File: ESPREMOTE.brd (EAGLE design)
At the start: 47 x 78 mm, 38 parts, among them IC1 ESP12SMT, J1 2.1MM DC Jack, Q1 2N7002, Q2 2N7002, Q3 2N7002, Q4 2N7002

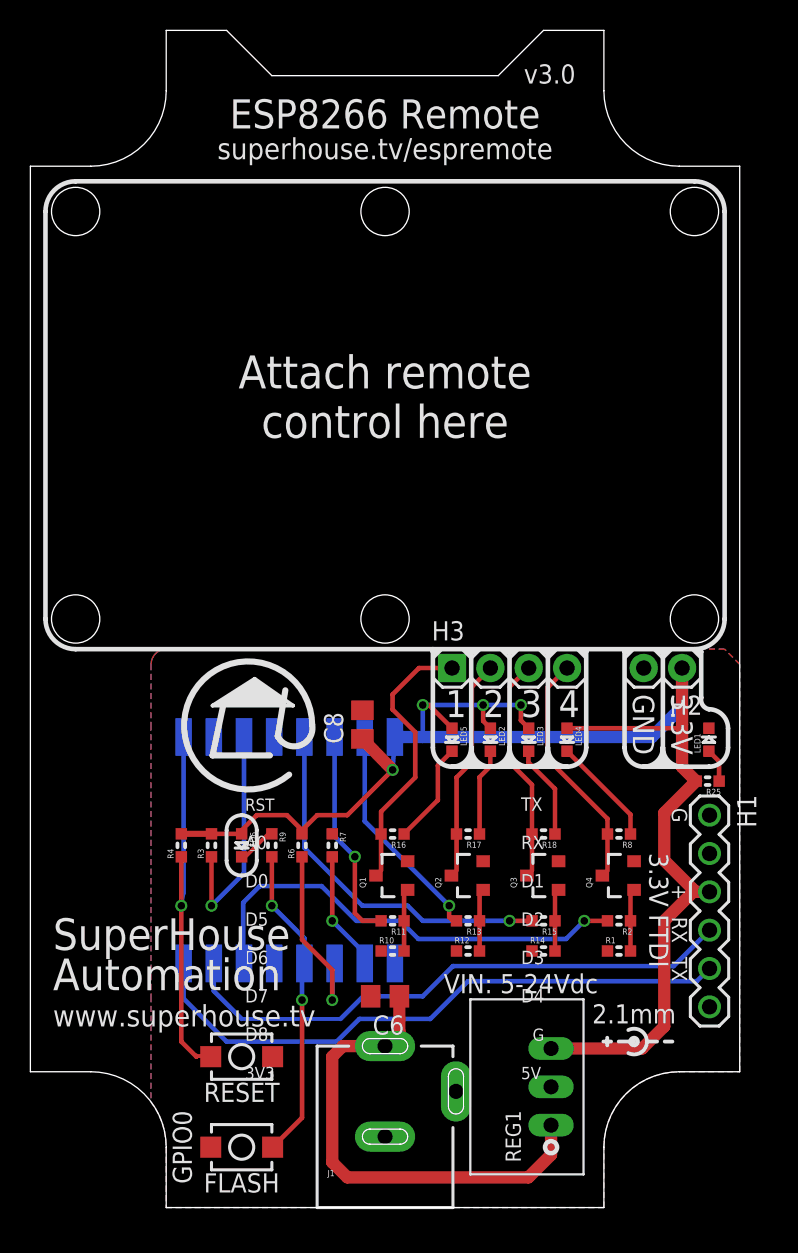
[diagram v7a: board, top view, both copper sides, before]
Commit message: Fixed ESP12 pinout for v3.1 release
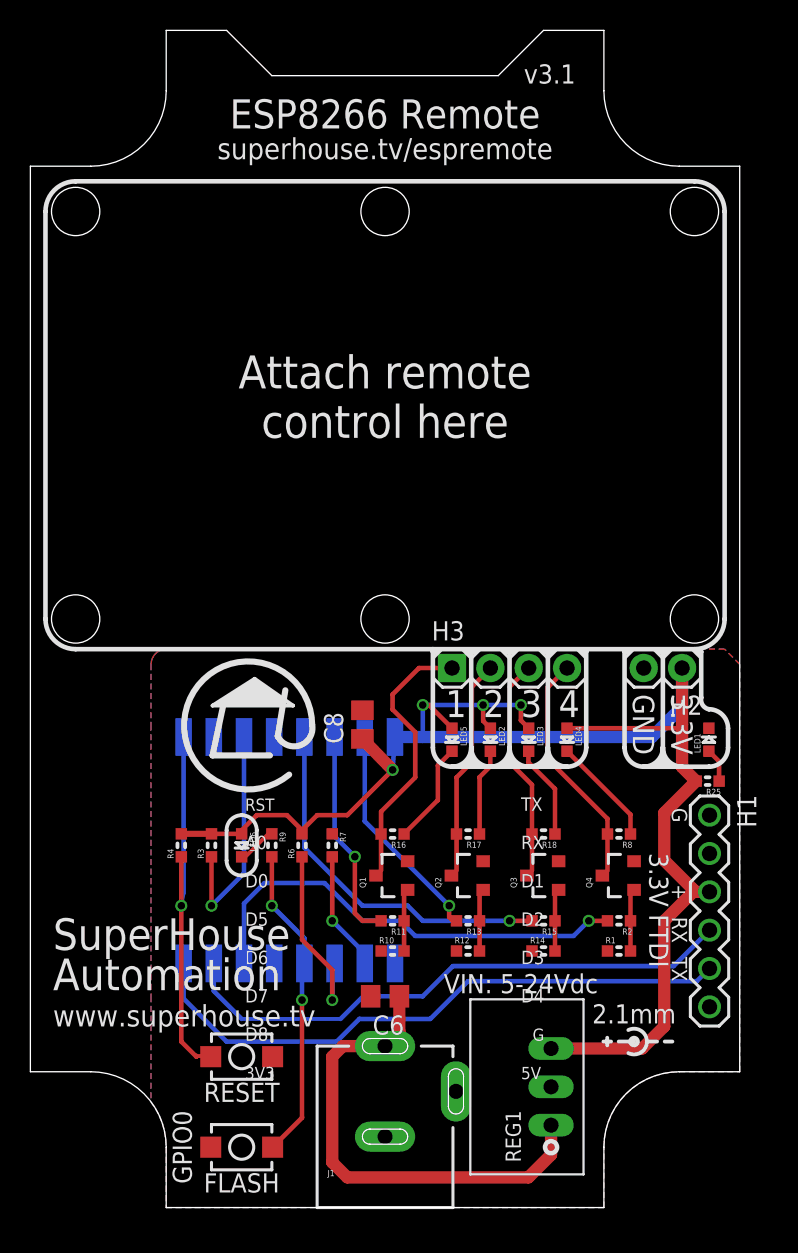
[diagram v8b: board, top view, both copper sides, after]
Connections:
- net GPIO4: now also IC1.13; no longer IC1.14, R2.2
- net GPIO5: now also IC1.14, R2.2; no longer IC1.13
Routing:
- net GPIO4: track 30.6 -> 0.00 mm, vias 1 -> 0
- net GPIO5: track 0.00 -> 30.5 mm, vias 0 -> 1
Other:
- board text added: "Output 1: GPIO12 Output 2: GPIO13 Output 3: GPIO14 Output 4: GPIO5"
- board text added: "v3.1"
- board text removed: "Output 1: GPIO12 Output 2: GPIO13 Output 3: GPIO14 Output 4: GPIO4"
- board text removed: "v3.0"
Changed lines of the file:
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@@
 <?xml version="1.0" encoding="utf-8"?>
 <!DOCTYPE eagle SYSTEM "eagle.dtd">
-<eagle version="8.6.0">
+<eagle version="8.7.0">
 <drawing>
 <settings>
@@
 <setting verticaltext="up"/>
 </settings>
-<grid distance="1" unitdist="mm" unit="mm" style="lines" multiple="1" display="yes" altdistance="5" altunitdist="mil" altunit="mil"/>
+<grid distance="0.5" unitdist="mm" unit="mm" style="lines" multiple="1" display="yes" altdistance="5" altunitdist="mil" altunit="mil"/>
 <layers>
 <layer number="1" name="Top" color="4" fill="1" visible="yes" active="yes"/>
@@
 <layer number="25" name="tNames" color="7" fill="1" visible="no" active="yes"/>
 <layer number="26" name="bNames" color="3" fill="1" visible="no" active="yes"/>
-<layer number="27" name="tValues" color="7" fill="1" visible="no" active="yes"/>
+<layer number="27" name="tValues" color="7" fill="1" visible="yes" active="yes"/>
 <layer number="28" name="bValues" color="3" fill="1" visible="no" active="yes"/>
 <layer number="29" name="tStop" color="7" fill="3" visible="no" active="yes"/>
@@
 <wire x1="14.354" y1="34.022" x2="14.862" y2="34.276" width="0.4064" layer="21"/>
 <text x="23.5" y="69.4632" size="1.4" layer="21" font="vector" ratio="15" rot="SR0" align="bottom-center">superhouse.tv/espremote</text>
-<text x="32.698" y="74.476" size="1.27" layer="21" font="vector" ratio="18">v3.0</text>
+<text x="32.698" y="74.476" size="1.27" layer="21" font="vector" ratio="18">v3.1</text>
 <text x="31.16" y="72.476" size="1.27" layer="22" font="vector" ratio="18" rot="MR0">SKU: ESPREMOTE</text>
 <hole x="44" y="39" drill="3.2"/>
@@
 Output 2: GPIO13
 Output 3: GPIO14
-Output 4: GPIO4</text>
+Output 4: GPIO5</text>
 <wire x1="39.619" y1="11.762" x2="39.619" y2="10.238" width="0.254" layer="21" curve="-233.130102"/>
 <circle x="40" y="11" radius="0.254" width="0.254" layer="21"/>
@@
 <attribute name="VALUE" x="31.9348" y="20.616" size="0.8128" layer="27" font="vector" rot="R270"/>
 </element>
-<element name="LED2" library="freetronics-master-v1" package="LED-0603" value="CH2/RED" x="30.48" y="31" rot="R270"/>
-<element name="LED3" library="freetronics-master-v1" package="LED-0603" value="CH3/RED" x="33.02" y="31" rot="R270"/>
-<element name="LED5" library="freetronics-master-v1" package="LED-0603" value="CH1/RED" x="27.94" y="31" rot="R270"/>
+<element name="LED2" library="freetronics-master-v1" package="LED-0603" value="CH2/RED" x="30.48" y="31" smashed="yes" rot="R270">
+<attribute name="NAME" x="31.0388" y="31.889" size="0.4064" layer="25" rot="R270"/>
+<attribute name="VALUE" x="29.5148" y="32.016" size="0.4064" layer="27" rot="R270"/>
+</element>
+<element name="LED3" library="freetronics-master-v1" package="LED-0603" value="CH3/RED" x="33.02" y="31" smashed="yes" rot="R270">
+<attribute name="NAME" x="33.5788" y="31.889" size="0.4064" layer="25" rot="R270"/>
+<attribute name="VALUE" x="32.0548" y="32.016" size="0.4064" layer="27" rot="R270"/>
+</element>
+<element name="LED5" library="freetronics-master-v1" package="LED-0603" value="CH1/RED" x="27.94" y="31" smashed="yes" rot="R270">
+<attribute name="NAME" x="28.4988" y="31.889" size="0.4064" layer="25" rot="R270"/>
+<attribute name="VALUE" x="26.9748" y="32.016" size="0.4064" layer="27" rot="R270"/>
+</element>
 <element name="R16" library="freetronics-master-v1" package="0603" value="1K" x="24" y="24.75" smashed="yes" rot="R180">
 <attribute name="NAME" x="24.889" y="24.242" size="0.4064" layer="25" font="vector" rot="R180"/>
@@
 <attribute name="VALUE" x="41.825" y="27.27" size="1.27" layer="27" rot="R270"/>
 </element>
-<element name="H2" library="freetronics-jon" package="1X02" value="" x="43.18" y="35.75" rot="R180"/>
-<element name="H3" library="freetronics-jon" package="1X04" value="" x="27.94" y="35.75"/>
+<element name="H2" library="freetronics-jon" package="1X02" value="" x="43.18" y="35.75" smashed="yes" rot="R180">
+<attribute name="NAME" x="44.5262" y="33.9212" size="1.27" layer="25" ratio="10" rot="R180"/>
+<attribute name="VALUE" x="44.45" y="38.925" size="1.27" layer="27" rot="R180"/>
+</element>
+<element name="H3" library="freetronics-jon" package="1X04" value="" x="27.94" y="35.75" smashed="yes">
+<attribute name="NAME" x="26.5938" y="37.5788" size="1.27" layer="25" ratio="10"/>
+<attribute name="VALUE" x="26.67" y="32.575" size="1.27" layer="27"/>
+</element>
 <element name="R1" library="freetronics-master-v1" package="0603" value="10K" x="39" y="17" smashed="yes">
 <attribute name="NAME" x="38.111" y="17.508" size="0.4064" layer="25" font="vector"/>
@@
 <attribute name="VALUE" x="39.2152" y="25.284" size="0.8128" layer="27" font="vector" rot="R90"/>
 </element>
-<element name="LED4" library="freetronics-master-v1" package="LED-0603" value="CH4/RED" x="35.56" y="31" rot="R270"/>
+<element name="LED4" library="freetronics-master-v1" package="LED-0603" value="CH4/RED" x="35.56" y="31" smashed="yes" rot="R270">
+<attribute name="NAME" x="36.1188" y="31.889" size="0.4064" layer="25" rot="R270"/>
+<attribute name="VALUE" x="34.5948" y="32.016" size="0.4064" layer="27" rot="R270"/>
+</element>
 <element name="R7" library="freetronics-jon" package="0603" value="10k" x="20" y="24" smashed="yes" rot="R270">
 <attribute name="NAME" x="20.508" y="24.889" size="0.4064" layer="25" font="vector" rot="R270"/>
@@
 <attribute name="VALUE" x="15.4652" y="22.284" size="0.8128" layer="27" font="vector" rot="R90"/>
 </element>
-<element name="C6" library="freetronics-jon" package="C0805" value="10uF 10V 0805" x="23.5" y="14" rot="R180"/>
-<element name="REG1" library="freetronics-jon" package="K78XX-500R3" value="K7803-500R3" x="34.5" y="8" rot="R90"/>
+<element name="C6" library="freetronics-jon" package="C0805" value="10uF 10V 0805" x="23.5" y="14" smashed="yes" rot="R180">
+<attribute name="NAME" x="24.77" y="12.73" size="1.27" layer="25" rot="R180"/>
+<attribute name="VALUE" x="21.54" y="9.23" size="0.8128" layer="27" rot="R90"/>
+</element>
+<element name="REG1" library="freetronics-jon" package="K78XX-500R3" value="K7803-500R3" x="34.5" y="8" smashed="yes" rot="R90">
+<attribute name="NAME" x="32.5" y="3" size="1.016" layer="25" rot="R90"/>
+<attribute name="VALUE" x="30" y="11.5" size="1.016" layer="27"/>
+</element>
 <element name="J1" library="freetronics-jon" package="POWER_JACK_PTH_SLOTS" value="2.1MM DC Jack" x="23.5" y="-3"/>
 </elements>
@@
 </signal>
 <signal name="GPIO5">
-<contactref element="IC1" pad="13"/>
-</signal>
-<signal name="GPIO4">
 <contactref element="IC1" pad="14"/>
 <contactref element="R2" pad="2"/>
-<wire x1="38.238" y1="19" x2="36.7" y2="19" width="0.3048" layer="1"/>
-<via x="36.7" y="19" extent="1-16" drill="0.5"/>
-<wire x1="36.7" y1="19" x2="35.5" y2="17.8" width="0.3048" layer="16"/>
-<wire x1="35.5" y1="17.8" x2="25.7" y2="17.8" width="0.3048" layer="16"/>
-<wire x1="25.7" y1="17.8" x2="24.5" y2="19" width="0.3048" layer="16"/>
-<wire x1="24.5" y1="19" x2="21.6" y2="19" width="0.3048" layer="16"/>
-<wire x1="21.6" y1="19" x2="19.3" y2="21.3" width="0.3048" layer="16"/>
-<wire x1="19.3" y1="21.3" x2="15.2" y2="21.3" width="0.3048" layer="16"/>
-<wire x1="15.2" y1="21.3" x2="14.1" y2="20.2" width="0.3048" layer="16"/>
-<wire x1="14.1" y1="20.2" x2="14.1" y2="16.232" width="0.3048" layer="16"/>
-<wire x1="14.1" y1="16.232" x2="14.154" y2="16.178" width="0.3048" layer="16"/>
+<wire x1="38.238" y1="19" x2="37" y2="19" width="0.3048" layer="1"/>
+<via x="37" y="19" extent="1-16" drill="0.5"/>
+<wire x1="37" y1="19" x2="36" y2="18" width="0.3048" layer="16"/>
+<wire x1="36" y1="18" x2="25.5" y2="18" width="0.3048" layer="16"/>
+<wire x1="25.5" y1="18" x2="24.5" y2="19" width="0.3048" layer="16"/>
+<wire x1="24.5" y1="19" x2="22" y2="19" width="0.3048" layer="16"/>
+<wire x1="22" y1="19" x2="19.5" y2="21.5" width="0.3048" layer="16"/>
+<wire x1="19.5" y1="21.5" x2="15.5" y2="21.5" width="0.3048" layer="16"/>
+<wire x1="14.154" y1="20.154" x2="14.154" y2="16.178" width="0.3048" layer="16"/>
+<wire x1="15.5" y1="21.5" x2="14.154" y2="20.154" width="0.3048" layer="16"/>
+</signal>
+<signal name="GPIO4">
+<contactref element="IC1" pad="13"/>
 </signal>
 <signal name="GPIO14">
@@
 </signal>
 </signals>
-<errors>
-</errors>
 </board>
 </drawing>
